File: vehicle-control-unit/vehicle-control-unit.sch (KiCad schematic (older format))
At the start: 23 parts

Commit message: Finish VCU schematic
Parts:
- JP1, JP2, JP3, JP4: renamed from JP?; symbol Jumper:Jumper_3_Bridged12 -> earth-rover-symbols:Jumper_3_Bridged12
- R5: renamed from R?; value R -> 10k
- U2: renamed from U?; value NRF24L01+ -> NRF24L01+ breakout
- gave numbers to parts that had none: 17
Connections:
- net labels added: GPS_SERIAL_RX, GPS_SERIAL_TX, THROTTLE, WINCH
- net labels removed: ESC, GPS_RX, GPS_TX, SPARE
- wire segments 162 -> 143
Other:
- note added: "Analog sensors"
- note added: "Automotive lighting (car and trailer connector)"
- note added: "Power supply\nBEC power supply can be used to switch power on and off"
- note added: "Reset EEPROM jumper\nClose and boot VCU to erase EEPROM"
- note added: "Servos\nJumpers select system 5V or BEC supply"
- note added: "Teensy 3.2 SOM"
- note removed: "Automotive lighting"
- note removed: "Power supply"
- note removed: "Reset EEPROM jumper"
- note removed: "Servos (jumpers select system 5V or BEC supply)"
- note removed: "Teensy 3.2"
- note removed: "Telemetry sensors"
- moved on the sheet: J1, J10, J11, J2, J3, J4, J5, J6, J7, J8, J9, JP5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

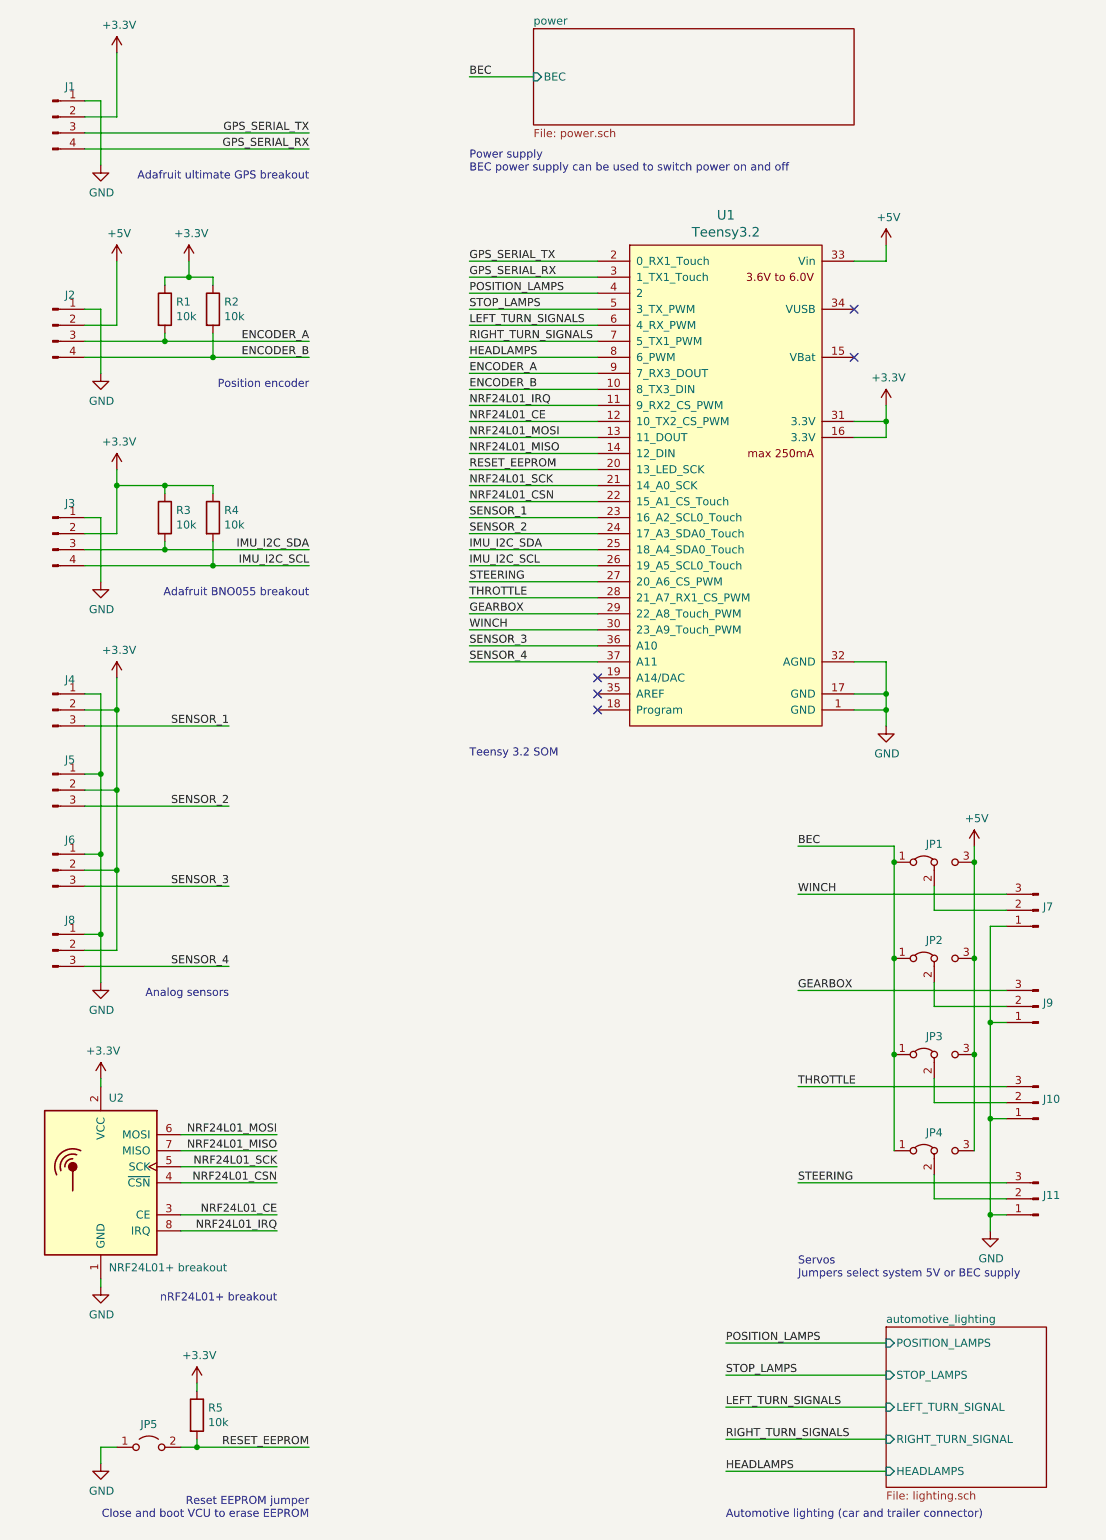
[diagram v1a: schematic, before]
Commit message: Improve layouts and add capacitors
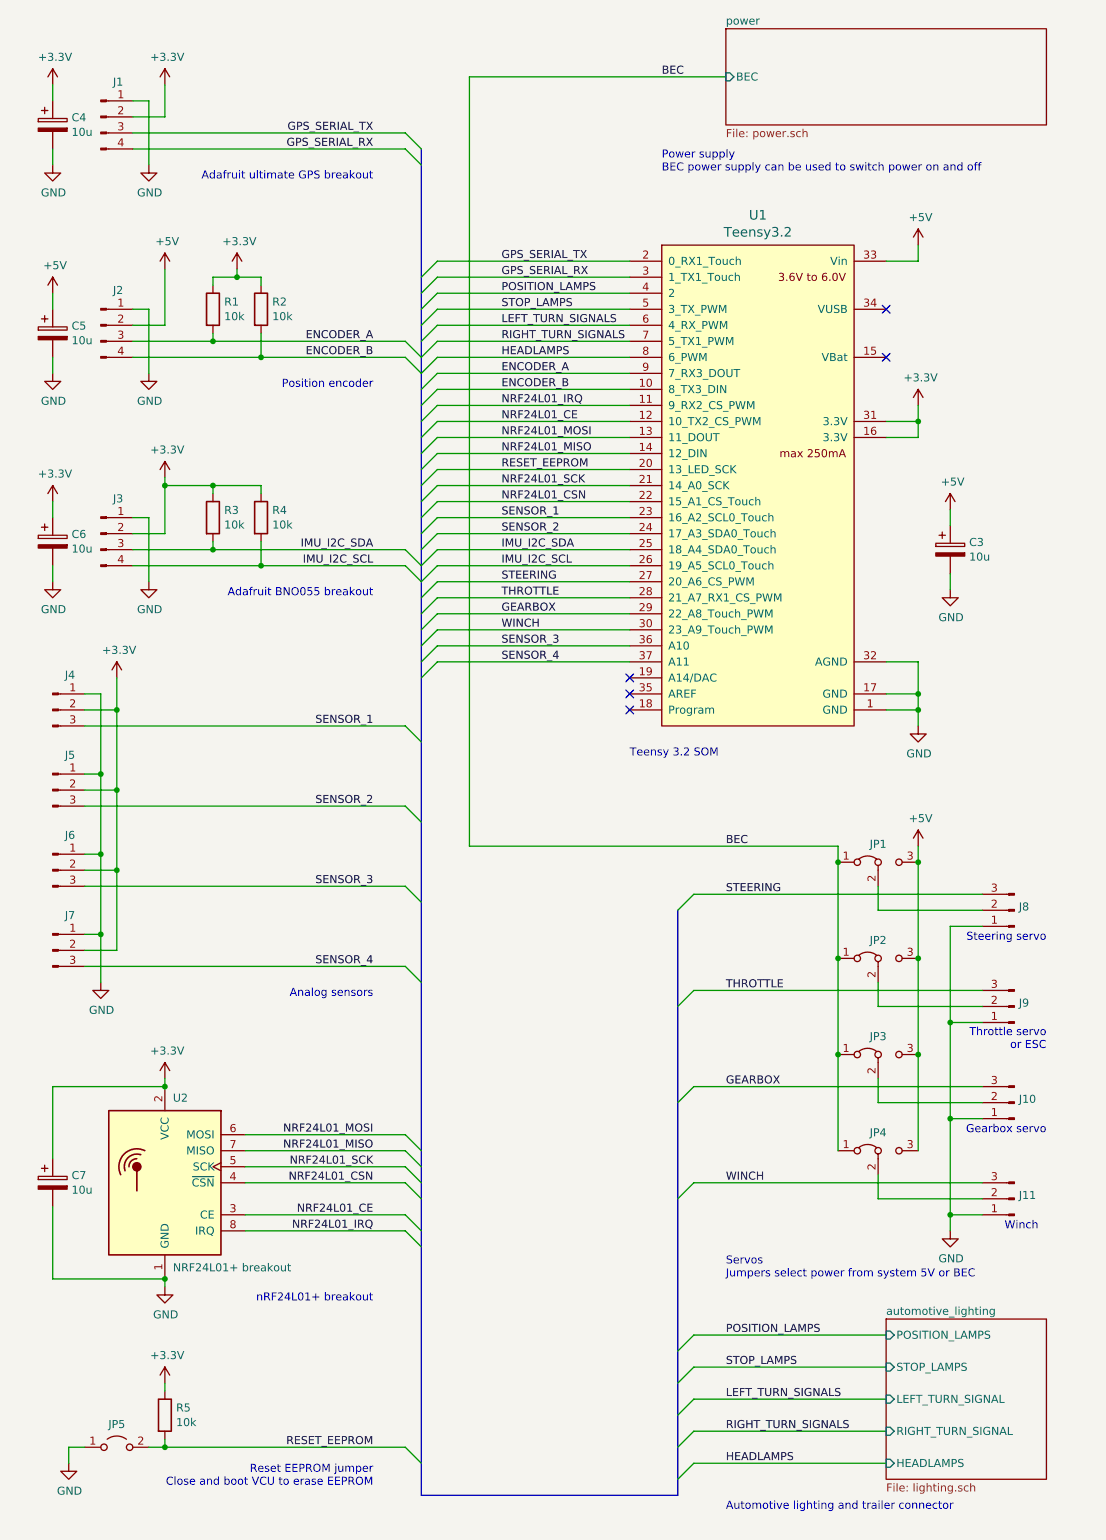
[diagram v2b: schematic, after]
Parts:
- added C3, C4, C5, C6, C7: 10u, symbol Device:CP
- renumbered J8 to J7, J7 to J8
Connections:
- net +3V3: now also C4.1, C6.1, C7.1
- net +5V: now also C3.1, C5.1
- net GEARBOX: now also J10.3 (Pin_3); no longer J9.3 (Pin_3)
- net GND: now also C3.2, C4.2, C5.2, C6.2, C7.2
- net STEERING: now also J8.3 (Pin_3); no longer J11.3 (Pin_3)
- net THROTTLE: now also J9.3 (Pin_3); no longer J10.3 (Pin_3)
- net WINCH: now also J11.3 (Pin_3); no longer J8.3 (Pin_3)
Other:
- note added: "Automotive lighting and trailer connector"
- note added: "Gearbox servo"
- note added: "Servos\nJumpers select power from system 5V or BEC"
- note added: "Steering servo"
- note added: "Throttle servo\nor ESC"
- note added: "Winch"
- note removed: "Automotive lighting (car and trailer connector)"
- note removed: "Servos\nJumpers select system 5V or BEC supply"
- moved on the sheet: J1, J10, J11, J2, J3, J8, J9, JP1, JP2, JP3, JP4, JP5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

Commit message: Review schematics
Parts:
- renumbered C4 to C1, C5 to C2, C6 to C3, C7 to C4, C3 to C5, J4 to J1, J5 to J2, J6 to J3, J7 to J4, J1 to J5, J2 to J6, J3 to J7, JP5 to JP1, JP1 to JP2, JP2 to JP3, JP3 to JP4, JP4 to JP5, R5 to R1, R1 to R2, R2 to R4, R4 to R5, U2 to U1, U1 to U2
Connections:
- net BATTERY_MONITOR: now reaches U2.19 (A14/DAC)
- no-connect marks 5 -> 4
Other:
- moved on the sheet: C5, U2

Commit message: Wire all turn signal LEDs in parallel
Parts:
- renumbered C5 to C4, C4 to C5, J5 to J1, J6 to J2, J7 to J3, J1 to J4, J2 to J5, J3 to J6, J8 to J7, J4 to J8, JP2 to JP1, JP3 to JP2, JP4 to JP3, JP5 to JP4, JP1 to JP5, R2 to R1, R4 to R2, R5 to R4, R1 to R5, U2 to U1, U1 to U2

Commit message: Assign footprints
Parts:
- C1, C2, C3, C4, C5: footprint (none) -> Capacitor_THT:CP_Radial_D5.0mm_P2.50mm
- J1, J2, J3: footprint (none) -> Connector_PinHeader_2.54mm:PinHeader_1x04_P2.54mm_Horizontal
- J10, J11, J4, J5, J6, J7, J8, J9: footprint (none) -> Connector_PinHeader_2.54mm:PinHeader_1x03_P2.54mm_Horizontal
- JP1, JP2, JP3, JP4: footprint (none) -> Connector_PinHeader_2.54mm:PinHeader_1x03_P2.54mm_Vertical
- JP5: footprint (none) -> Connector_PinHeader_2.54mm:PinHeader_1x02_P2.54mm_Vertical
- R1, R2, R3, R4, R5: footprint (none) -> Resistor_THT:R_Axial_DIN0207_L6.3mm_D2.5mm_P10.16mm_Horizontal
- U1: footprint (none) -> earth-rover-footprints:Teensy_3.2_with_USB_connector
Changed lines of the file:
@@
 F 0 "J7" H 7222 6228 50  0000 R CNN
 F 1 "Conn_01x03_Male" H 7222 6273 50  0001 R CNN
-F 2 "" H 7250 6250 50  0001 C CNN
+F 2 "Connector_PinHeader_2.54mm:PinHeader_1x03_P2.54mm_Horizontal" H 7250 6250 50  0001 C CNN
 F 3 "~" H 7250 6250 50  0001 C CNN
 	1    7250 6250
@@
 F 0 "J9" H 7222 6828 50  0000 R CNN
 F 1 "Conn_01x03_Male" H 7222 6873 50  0001 R CNN
-F 2 "" H 7250 6850 50  0001 C CNN
+F 2 "Connector_PinHeader_2.54mm:PinHeader_1x03_P2.54mm_Horizontal" H 7250 6850 50  0001 C CNN
 F 3 "~" H 7250 6850 50  0001 C CNN
 	1    7250 6850
@@
 F 0 "J10" H 7222 7428 50  0000 R CNN
 F 1 "Conn_01x03_Male" H 7222 7473 50  0001 R CNN
-F 2 "" H 7250 7450 50  0001 C CNN
+F 2 "Connector_PinHeader_2.54mm:PinHeader_1x03_P2.54mm_Horizontal" H 7250 7450 50  0001 C CNN
 F 3 "~" H 7250 7450 50  0001 C CNN
 	1    7250 7450
@@
 F 0 "J11" H 7222 8028 50  0000 R CNN
 F 1 "Conn_01x03_Male" H 7222 8073 50  0001 R CNN
-F 2 "" H 7250 8050 50  0001 C CNN
+F 2 "Connector_PinHeader_2.54mm:PinHeader_1x03_P2.54mm_Horizontal" H 7250 8050 50  0001 C CNN
 F 3 "~" H 7250 8050 50  0001 C CNN
 	1    7250 8050
@@
 F 0 "JP1" H 6400 6063 50  0000 C CNN
 F 1 "Jumper_3_Bridged12" H 6400 6063 50  0001 C CNN
-F 2 "" H 6400 5950 50  0001 C CNN
+F 2 "Connector_PinHeader_2.54mm:PinHeader_1x03_P2.54mm_Vertical" H 6400 5950 50  0001 C CNN
 F 3 "~" H 6400 5950 50  0001 C CNN
 	1    6400 5950
@@
 F 0 "JP2" H 6400 6663 50  0000 C CNN
 F 1 "Jumper_3_Bridged12" H 6400 6663 50  0001 C CNN
-F 2 "" H 6400 6550 50  0001 C CNN
+F 2 "Connector_PinHeader_2.54mm:PinHeader_1x03_P2.54mm_Vertical" H 6400 6550 50  0001 C CNN
 F 3 "~" H 6400 6550 50  0001 C CNN
 	1    6400 6550
@@
 F 0 "JP3" H 6400 7263 50  0000 C CNN
 F 1 "Jumper_3_Bridged12" H 6400 7263 50  0001 C CNN
-F 2 "" H 6400 7150 50  0001 C CNN
+F 2 "Connector_PinHeader_2.54mm:PinHeader_1x03_P2.54mm_Vertical" H 6400 7150 50  0001 C CNN
 F 3 "~" H 6400 7150 50  0001 C CNN
 	1    6400 7150
@@
 F 0 "JP4" H 6400 7863 50  0000 C CNN
 F 1 "Jumper_3_Bridged12" H 6400 7863 50  0001 C CNN
-F 2 "" H 6400 7750 50  0001 C CNN
+F 2 "Connector_PinHeader_2.54mm:PinHeader_1x03_P2.54mm_Vertical" H 6400 7750 50  0001 C CNN
 F 3 "~" H 6400 7750 50  0001 C CNN
 	1    6400 7750
@@
 F 0 "U1" H 5850 2487 60  0000 C CNN
 F 1 "Teensy3.2" H 5850 2381 60  0000 C CNN
-F 2 "" H 8650 1050 60  0000 C CNN
+F 2 "earth-rover-footprints:Teensy_3.2_with_USB_connector" H 8650 1050 60  0001 C CNN
 F 3 "" H 8650 1050 60  0000 C CNN
 	1    5250 2200
@@
 F 0 "J4" H 1358 5189 50  0000 C BNN
 F 1 "Conn_01x03_Male" H 1358 5190 50  0001 C CNN
-F 2 "" H 1250 5000 50  0001 C CNN
+F 2 "Connector_PinHeader_2.54mm:PinHeader_1x03_P2.54mm_Horizontal" H 1250 5000 50  0001 C CNN
 F 3 "~" H 1250 5000 50  0001 C CNN
 	1    1250 5000
@@
 F 0 "J5" H 1358 5689 50  0000 C BNN
 F 1 "Conn_01x03_Male" H 1358 5690 50  0001 C CNN
-F 2 "" H 1250 5500 50  0001 C CNN
+F 2 "Connector_PinHeader_2.54mm:PinHeader_1x03_P2.54mm_Horizontal" H 1250 5500 50  0001 C CNN
 F 3 "~" H 1250 5500 50  0001 C CNN
 	1    1250 5500
@@
 F 0 "J6" H 1358 6189 50  0000 C BNN
 F 1 "Conn_01x03_Male" H 1358 6190 50  0001 C CNN
-F 2 "" H 1250 6000 50  0001 C CNN
+F 2 "Connector_PinHeader_2.54mm:PinHeader_1x03_P2.54mm_Horizontal" H 1250 6000 50  0001 C CNN
 F 3 "~" H 1250 6000 50  0001 C CNN
 	1    1250 6000
@@
 F 0 "J8" H 1358 6689 50  0000 C BNN
 F 1 "Conn_01x03_Male" H 1358 6690 50  0001 C CNN
-F 2 "" H 1250 6500 50  0001 C CNN
+F 2 "Connector_PinHeader_2.54mm:PinHeader_1x03_P2.54mm_Horizontal" H 1250 6500 50  0001 C CNN
 F 3 "~" H 1250 6500 50  0001 C CNN
 	1    1250 6500
@@
 F 0 "JP5" H 1650 9743 50  0000 C CNN
 F 1 "Jumper_2_Open" V 1695 9698 50  0001 L CNN
-F 2 "" H 1650 9600 50  0001 C CNN
+F 2 "Connector_PinHeader_2.54mm:PinHeader_1x02_P2.54mm_Vertical" H 1650 9600 50  0001 C CNN
 F 3 "~" H 1650 9600 50  0001 C CNN
 	1    1650 9600
@@
 F 0 "J1" H 1658 1489 50  0000 C BNN
 F 1 "Conn_01x04_Male" H 1658 1490 50  0001 C CNN
-F 2 "" H 1550 1300 50  0001 C CNN
+F 2 "Connector_PinHeader_2.54mm:PinHeader_1x04_P2.54mm_Horizontal" H 1550 1300 50  0001 C CNN
 F 3 "~" H 1550 1300 50  0001 C CNN
 	1    1550 1300
@@
 F 0 "R4" H 2620 3846 50  0000 L CNN
 F 1 "10k" H 2620 3755 50  0000 L CNN
-F 2 "" V 2480 3800 50  0001 C CNN
+F 2 "Resistor_THT:R_Axial_DIN0207_L6.3mm_D2.5mm_P10.16mm_Horizontal" V 2480 3800 50  0001 C CNN
 F 3 "~" H 2550 3800 50  0001 C CNN
 	1    2550 3800
@@
 F 0 "R3" H 2320 3846 50  0000 L CNN
 F 1 "10k" H 2320 3755 50  0000 L CNN
-F 2 "" V 2180 3800 50  0001 C CNN
+F 2 "Resistor_THT:R_Axial_DIN0207_L6.3mm_D2.5mm_P10.16mm_Horizontal" V 2180 3800 50  0001 C CNN
 F 3 "~" H 2250 3800 50  0001 C CNN
 	1    2250 3800
@@
 F 0 "J3" H 1658 4089 50  0000 C BNN
 F 1 "Conn_01x04_Male" H 1658 4090 50  0001 C CNN
-F 2 "" H 1550 3900 50  0001 C CNN
+F 2 "Connector_PinHeader_2.54mm:PinHeader_1x04_P2.54mm_Horizontal" H 1550 3900 50  0001 C CNN
 F 3 "~" H 1550 3900 50  0001 C CNN
 	1    1550 3900
@@
 F 0 "R2" H 2620 2546 50  0000 L CNN
 F 1 "10k" H 2620 2455 50  0000 L CNN
-F 2 "" V 2480 2500 50  0001 C CNN
+F 2 "Resistor_THT:R_Axial_DIN0207_L6.3mm_D2.5mm_P10.16mm_Horizontal" V 2480 2500 50  0001 C CNN
 F 3 "~" H 2550 2500 50  0001 C CNN
 	1    2550 2500
@@
 F 0 "R1" H 2320 2546 50  0000 L CNN
 F 1 "10k" H 2320 2455 50  0000 L CNN
-F 2 "" V 2180 2500 50  0001 C CNN
+F 2 "Resistor_THT:R_Axial_DIN0207_L6.3mm_D2.5mm_P10.16mm_Horizontal" V 2180 2500 50  0001 C CNN
 F 3 "~" H 2250 2500 50  0001 C CNN
 	1    2250 2500
@@
 F 0 "J2" H 1658 2789 50  0000 C BNN
 F 1 "Conn_01x04_Male" H 1658 2790 50  0001 C CNN
-F 2 "" H 1550 2600 50  0001 C CNN
+F 2 "Connector_PinHeader_2.54mm:PinHeader_1x04_P2.54mm_Horizontal" H 1550 2600 50  0001 C CNN
 F 3 "~" H 1550 2600 50  0001 C CNN
 	1    1550 2600
@@
 F 0 "R5" H 2020 9446 50  0000 L CNN
 F 1 "10k" H 2020 9355 50  0000 L CNN
-F 2 "" V 1880 9400 50  0001 C CNN
+F 2 "Resistor_THT:R_Axial_DIN0207_L6.3mm_D2.5mm_P10.16mm_Horizontal" V 1880 9400 50  0001 C CNN
 F 3 "~" H 1950 9400 50  0001 C CNN
 	1    1950 9400
@@
 F 0 "C5" H 1368 7996 50  0000 L CNN
 F 1 "10u" H 1368 7905 50  0000 L CNN
-F 2 "" H 1288 7800 50  0001 C CNN
+F 2 "Capacitor_THT:CP_Radial_D5.0mm_P2.50mm" H 1288 7800 50  0001 C CNN
 F 3 "~" H 1250 7950 50  0001 C CNN
 	1    1250 7950
@@
 F 0 "C4" H 7168 4046 50  0000 L CNN
 F 1 "10u" H 7168 3955 50  0000 L CNN
-F 2 "" H 7088 3850 50  0001 C CNN
+F 2 "Capacitor_THT:CP_Radial_D5.0mm_P2.50mm" H 7088 3850 50  0001 C CNN
 F 3 "~" H 7050 4000 50  0001 C CNN
 	1    7050 4000
@@
 F 0 "C3" H 1368 3996 50  0000 L CNN
 F 1 "10u" H 1368 3905 50  0000 L CNN
-F 2 "" H 1288 3800 50  0001 C CNN
+F 2 "Capacitor_THT:CP_Radial_D5.0mm_P2.50mm" H 1288 3800 50  0001 C CNN
 F 3 "~" H 1250 3950 50  0001 C CNN
 	1    1250 3950
@@
 F 0 "C1" H 1368 1396 50  0000 L CNN
 F 1 "10u" H 1368 1305 50  0000 L CNN
-F 2 "" H 1288 1200 50  0001 C CNN
+F 2 "Capacitor_THT:CP_Radial_D5.0mm_P2.50mm" H 1288 1200 50  0001 C CNN
 F 3 "~" H 1250 1350 50  0001 C CNN
 	1    1250 1350
@@
 F 0 "C2" H 1368 2696 50  0000 L CNN
 F 1 "10u" H 1368 2605 50  0000 L CNN
-F 2 "" H 1288 2500 50  0001 C CNN
+F 2 "Capacitor_THT:CP_Radial_D5.0mm_P2.50mm" H 1288 2500 50  0001 C CNN
 F 3 "~" H 1250 2650 50  0001 C CNN
 	1    1250 2650

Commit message: Route PCB
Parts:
- removed C3: 10u, Capacitor_THT:CP_Radial_D5.0mm_P2.50mm, symbol Device:CP
- J1: renamed from J3; value Conn_01x04_Male -> Conn_02x04_Male_UnitPerRow; footprint Connector_PinHeader_2.54mm:PinHeader_1x04_P2.54mm_Horizontal -> Connector_PinHeader_2.54mm:PinHeader_2x04_P2.54mm_Horizontal; symbol Connector:Conn_01x04_Male -> earth-rover-symbols:Conn_02x04_Male_UnitPerRow
- J1: value Conn_01x04_Male -> Conn_02x04_Male_UnitPerRow; footprint Connector_PinHeader_2.54mm:PinHeader_1x04_P2.54mm_Horizontal -> Connector_PinHeader_2.54mm:PinHeader_2x04_P2.54mm_Horizontal; symbol Connector:Conn_01x04_Male -> earth-rover-symbols:Conn_02x04_Male_UnitPerRow
- J3: renamed from J4; value Conn_01x03_Male -> Conn_02x03_Male; footprint Connector_PinHeader_2.54mm:PinHeader_1x03_P2.54mm_Horizontal -> Connector_PinHeader_2.54mm:PinHeader_2x03_P2.54mm_Horizontal; symbol Connector:Conn_01x03_Male -> earth-rover-symbols:Conn_02x03_Male_UnitPerRow
- J3: renamed from J5; value Conn_01x03_Male -> Conn_02x03_Male; footprint Connector_PinHeader_2.54mm:PinHeader_1x03_P2.54mm_Horizontal -> Connector_PinHeader_2.54mm:PinHeader_2x03_P2.54mm_Horizontal; symbol Connector:Conn_01x03_Male -> earth-rover-symbols:Conn_02x03_Male_UnitPerRow
- J4: renamed from J6; value Conn_01x03_Male -> Conn_02x03_Male; footprint Connector_PinHeader_2.54mm:PinHeader_1x03_P2.54mm_Horizontal -> Connector_PinHeader_2.54mm:PinHeader_2x03_P2.54mm_Horizontal; symbol Connector:Conn_01x03_Male -> earth-rover-symbols:Conn_02x03_Male_UnitPerRow
- J4: renamed from J8; value Conn_01x03_Male -> Conn_02x03_Male; footprint Connector_PinHeader_2.54mm:PinHeader_1x03_P2.54mm_Horizontal -> Connector_PinHeader_2.54mm:PinHeader_2x03_P2.54mm_Horizontal; symbol Connector:Conn_01x03_Male -> earth-rover-symbols:Conn_02x03_Male_UnitPerRow
- J5: renamed from J7; value Conn_01x03_Male -> Conn_02x03_Male; footprint Connector_PinHeader_2.54mm:PinHeader_1x03_P2.54mm_Horizontal -> Connector_PinHeader_2.54mm:PinHeader_2x03_P2.54mm_Horizontal; symbol Connector:Conn_01x03_Male -> earth-rover-symbols:Conn_02x03_Male_UnitPerRow
- J5: renamed from J9; value Conn_01x03_Male -> Conn_02x03_Male; footprint Connector_PinHeader_2.54mm:PinHeader_1x03_P2.54mm_Horizontal -> Connector_PinHeader_2.54mm:PinHeader_2x03_P2.54mm_Horizontal; symbol Connector:Conn_01x03_Male -> earth-rover-symbols:Conn_02x03_Male_UnitPerRow
- J6: renamed from J10; value Conn_01x03_Male -> Conn_02x03_Male; footprint Connector_PinHeader_2.54mm:PinHeader_1x03_P2.54mm_Horizontal -> Connector_PinHeader_2.54mm:PinHeader_2x03_P2.54mm_Horizontal; symbol Connector:Conn_01x03_Male -> earth-rover-symbols:Conn_02x03_Male_UnitPerRow
- J6: renamed from J11; value Conn_01x03_Male -> Conn_02x03_Male; footprint Connector_PinHeader_2.54mm:PinHeader_1x03_P2.54mm_Horizontal -> Connector_PinHeader_2.54mm:PinHeader_2x03_P2.54mm_Horizontal; symbol Connector:Conn_01x03_Male -> earth-rover-symbols:Conn_02x03_Male_UnitPerRow
- U1: footprint earth-rover-footprints:Teensy_3.2_with_USB_connector -> earth-rover-footprints:Teensy_3.2
- renumbered C4 to C3, C5 to C4, R3 to R1, R4 to R2, R1 to R3, R2 to R4
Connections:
- net +3V3: now also J1.3 (Pin_3), J1.4 (Pin_4), J3.3 (Pin_3), J3.4 (Pin_4), J4.3 (Pin_3), J4.4 (Pin_4); no longer J1.2 (Pin_2), J1.2 (Pin_2), J3.2 (Pin_2), J3.2 (Pin_2), J4.2 (Pin_2), J4.2 (Pin_2)
- net GEARBOX: now also J6.5 (Pin_5); no longer J6.3 (Pin_3)
- net GND: now also J1.2 (Pin_2), J3.2 (Pin_2), J4.2 (Pin_2), J5.2 (Pin_2), J6.2 (Pin_2); no longer J1.1 (Pin_1), J3.1 (Pin_1), J4.1 (Pin_1), J5.1 (Pin_1), J6.1 (Pin_1)
- net GPS_SERIAL_RX: now also J1.8 (Pin_8); no longer J1.4 (Pin_4)
- net GPS_SERIAL_TX: now also J1.6 (Pin_6); no longer J1.3 (Pin_3)
- net IMU_I2C_SCL: now also J1.7 (Pin_7); no longer J1.4 (Pin_4)
- net IMU_I2C_SDA: now also J1.5 (Pin_5); no longer J1.3 (Pin_3)
- net SENSOR_1: now also J3.6 (Pin_6), U1.36 (A10); no longer J3.3 (Pin_3), U1.23 (16_A2_SCL0_Touch)
- net SENSOR_2: now also J3.5 (Pin_5), U1.37 (A11); no longer J3.3 (Pin_3), U1.24 (17_A3_SDA0_Touch)
- net SENSOR_3: now also J4.6 (Pin_6), U1.24 (17_A3_SDA0_Touch); no longer J4.3 (Pin_3), U1.36 (A10)
- net SENSOR_4: now also J4.5 (Pin_5), U1.23 (16_A2_SCL0_Touch); no longer J4.3 (Pin_3), U1.37 (A11)
- net STEERING: now also J5.5 (Pin_5); no longer J5.3 (Pin_3)
- net THROTTLE: now also J5.6 (Pin_6); no longer J5.3 (Pin_3)
- net WINCH: now also J6.6 (Pin_6); no longer J6.3 (Pin_3)
- net at JP1.2 (C): now also J5.3 (Pin_3); no longer J5.2 (Pin_2)
- net at JP2.2 (C): now also J5.4 (Pin_4); no longer J5.2 (Pin_2)
- net at JP3.2 (C): now also J6.3 (Pin_3); no longer J6.2 (Pin_2)
- net at JP4.2 (C): now also J6.4 (Pin_4); no longer J6.2 (Pin_2)
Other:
- moved on the sheet: C1, C2, J1A, J2, R1, R2, R3, R4
